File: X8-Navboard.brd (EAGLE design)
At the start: 35.3 x 47 mm, 14 parts, among them U1 MS5803-14BA

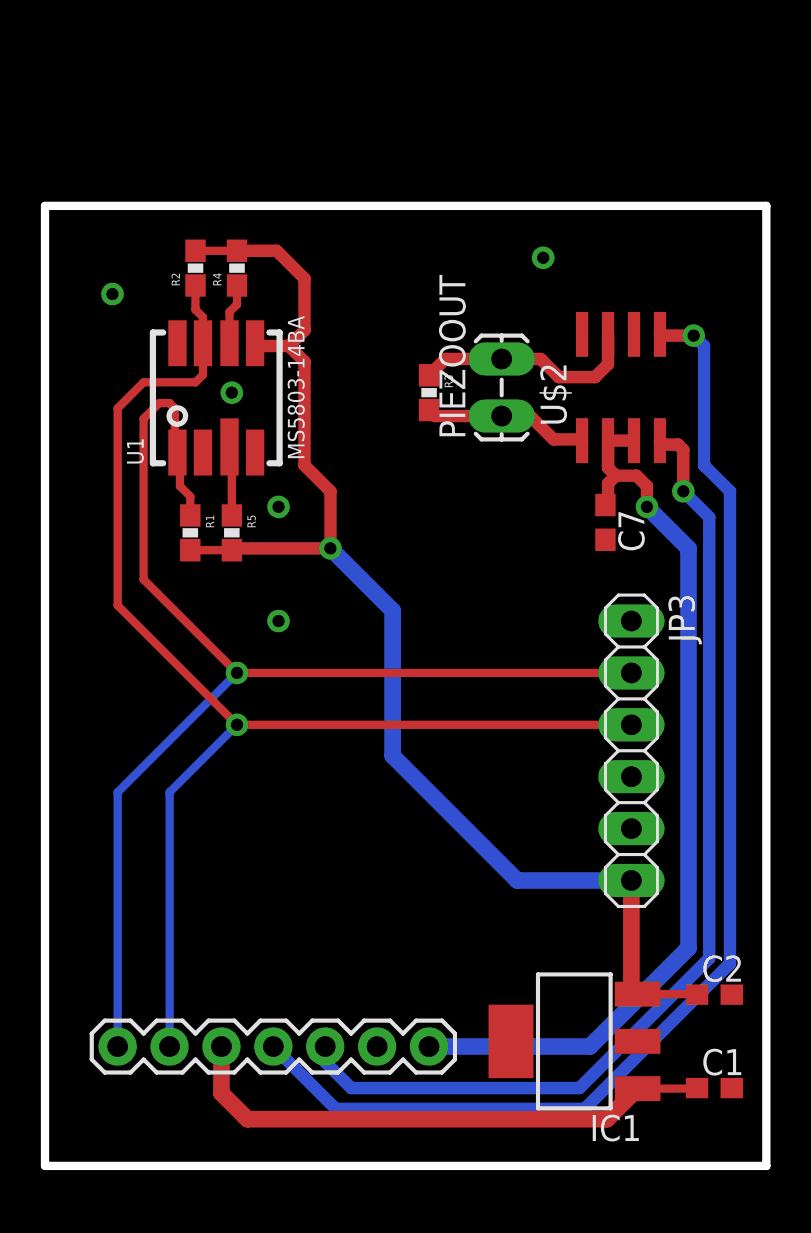
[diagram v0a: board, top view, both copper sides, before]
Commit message: Finished the board layout for the nav board
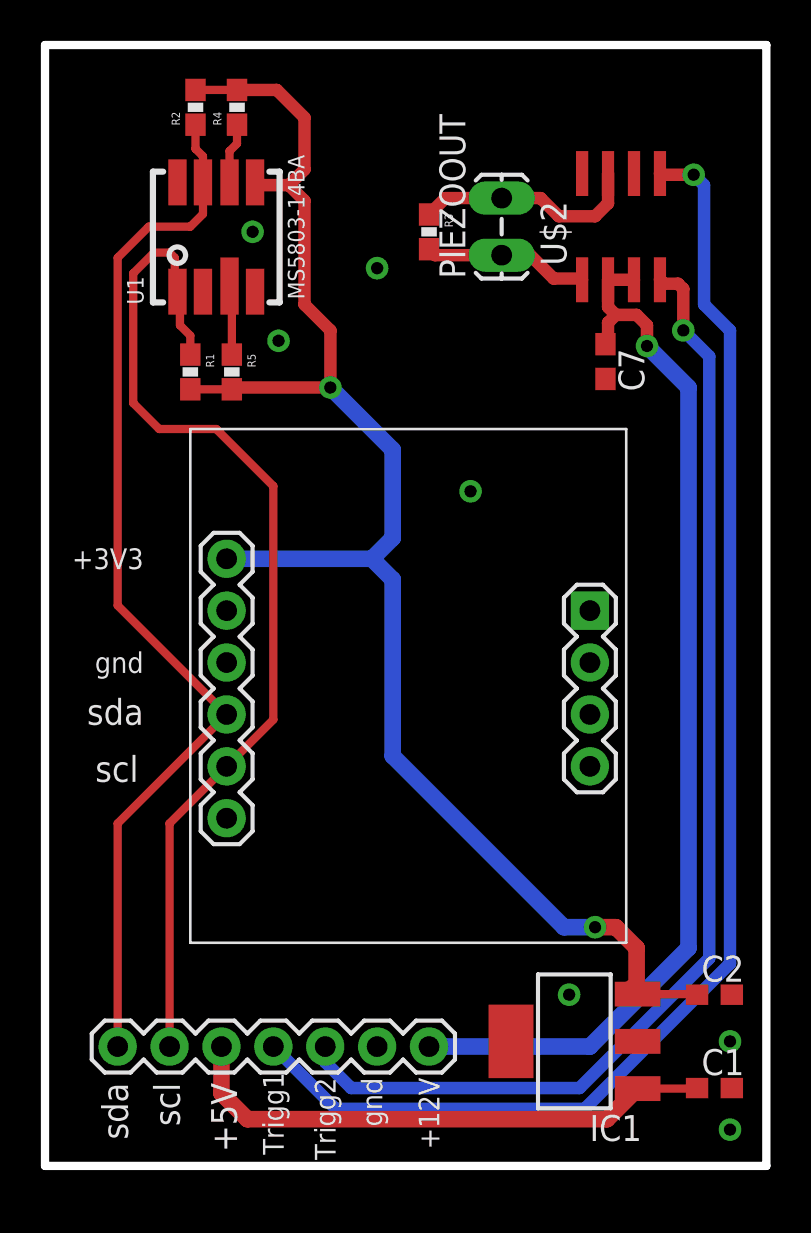
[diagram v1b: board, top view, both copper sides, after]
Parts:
- removed JP3: (no value), pinhead:1X06
- added U$1: BNO055_9DOF_BREAKOUT, Other:BNO055
- moved PIEZOOUT 7.87 mm to (22.4, 44.7)
- moved R1 7.87 mm to (7.11, 38.9)
- moved R2 7.87 mm to (7.37, 51.8)
- moved R3 7.87 mm to (18.8, 45.7)
- moved R4 7.87 mm to (9.40, 51.8)
- moved R5 7.87 mm to (9.14, 38.9)
- moved U1 7.87 mm to (8.38, 45.5)
- moved C7 7.87 mm to (27.4, 39.4)
- moved U$2 7.87 mm to (28.2, 46.0)
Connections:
- net 3.3V: now also U$1.VIN; no longer JP3.6
- net GND: now also U$1.GND; no longer JP3.4
- net SCL/SCLK: now also JP1.2, U$1.SCL; no longer JP1.1, JP3.2
- net SDA/SDI: now also JP1.1, U$1.SDA; no longer JP1.2, JP3.3
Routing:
- net 3.3V: track 63.1 -> 77.7 mm, vias 1 -> 2
- net SDA/SDI: track 63.7 -> 52.6 mm, vias 1 -> 0
- net SCL/SCLK: track 61.9 -> 52.0 mm, vias 1 -> 0
- net TRIGG2: track 49.5 -> 57.3 mm
- net TRIGG1: track 59.7 -> 67.6 mm
- net +12V: track 44.7 -> 52.5 mm
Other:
- board size 35.3 x 47 mm -> 35.3 x 54.9 mm
- board text added: "+12V"
- board text added: "+3V3"
- board text added: "+5V"
- board text added: "Trigg1"
- board text added: "Trigg2"
- board text added: "gnd"
- board text added: "scl"
- board text added: "sda"
